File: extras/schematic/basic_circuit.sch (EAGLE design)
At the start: 17 parts, among them M1 ARDUINO-PRO-MINI-3.3V, Y1 32.768kHz

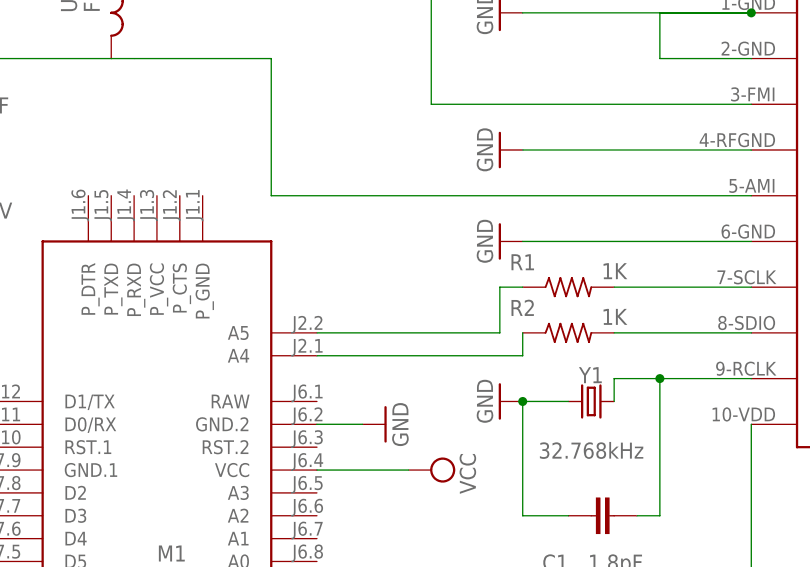
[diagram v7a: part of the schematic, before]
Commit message: BK1088 Arduino Library
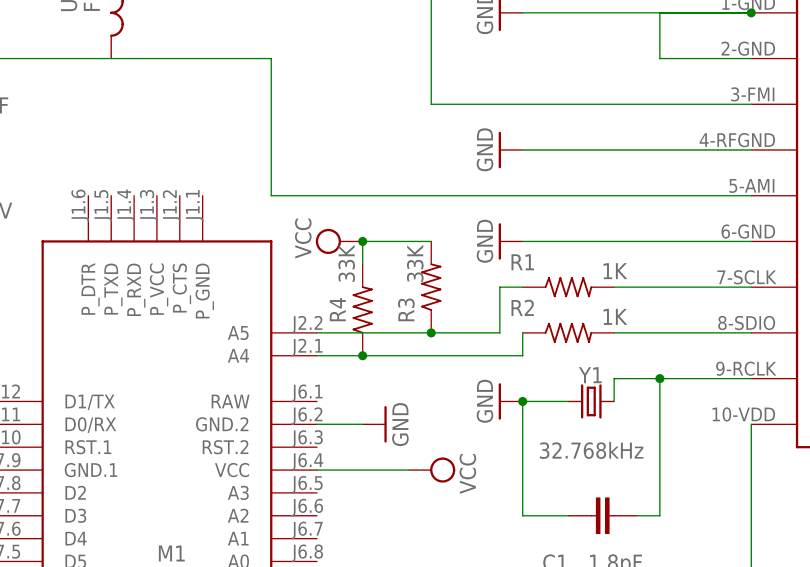
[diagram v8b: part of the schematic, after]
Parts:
- added R3, R4: 33K, Resistor:R-US_AXIAL-7.2MM-PITCH
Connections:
- net N$3: now also R4.1
- net N$4: now also R3.1
- net VCC: now also R3.2, R4.2
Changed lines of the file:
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@@
 <drawing>
 <settings>
-<setting alwaysvectorfont="yes"/>
+<setting alwaysvectorfont="no"/>
 <setting verticaltext="up"/>
 </settings>
@@
 <part name="C6" library="capacitor-wima" library_urn="urn:adsk.eagle:library:116" deviceset="C" device="5/3" package3d_urn="urn:adsk.eagle:package:5433/1" value="100nF"/>
 <part name="SW" library="discrete" library_urn="urn:adsk.eagle:library:211" deviceset="ANTENNA" device="" package3d_urn="urn:adsk.eagle:package:12928/1"/>
+<part name="R3" library="Resistor" library_urn="urn:adsk.eagle:library:16378527" deviceset="R-US" device="AXIAL-7.2MM-PITCH" package3d_urn="urn:adsk.eagle:package:16378561/2" technology="_" value="33K"/>
+<part name="R4" library="Resistor" library_urn="urn:adsk.eagle:library:16378527" deviceset="R-US" device="AXIAL-7.2MM-PITCH" package3d_urn="urn:adsk.eagle:package:16378561/2" technology="_" value="33K"/>
+<part name="SUPPLY3" library="supply2" library_urn="urn:adsk.eagle:library:372" deviceset="VCC" device=""/>
 </parts>
 <sheets>
@@
 <attribute name="NAME" x="-66.04" y="80.01" size="1.778" layer="95"/>
 <attribute name="VALUE" x="-60.96" y="73.66" size="1.778" layer="96"/>
+</instance>
+<instance part="R3" gate="G$1" x="12.7" y="45.72" smashed="yes" rot="R90">
+<attribute name="NAME" x="9.9314" y="43.18" size="1.778" layer="95" rot="R90" align="center"/>
+<attribute name="VALUE" x="10.922" y="48.26" size="1.778" layer="96" rot="R90" align="center"/>
+</instance>
+<instance part="R4" gate="G$1" x="5.08" y="43.18" smashed="yes" rot="R90">
+<attribute name="NAME" x="2.3114" y="43.18" size="1.778" layer="95" rot="R90" align="center"/>
+<attribute name="VALUE" x="3.302" y="48.26" size="1.778" layer="96" rot="R90" align="center"/>
+</instance>
+<instance part="SUPPLY3" gate="G$1" x="2.54" y="50.8" smashed="yes" rot="R90">
+<attribute name="VALUE" x="-0.635" y="48.895" size="1.778" layer="96" rot="R90"/>
 </instance>
 </instances>
@@
 <junction x="119.38" y="12.7"/>
 </segment>
+<segment>
+<pinref part="R4" gate="G$1" pin="2"/>
+<wire x1="5.08" y1="48.26" x2="5.08" y2="50.8" width="0.1524" layer="91"/>
+<pinref part="R3" gate="G$1" pin="2"/>
+<wire x1="5.08" y1="50.8" x2="12.7" y2="50.8" width="0.1524" layer="91"/>
+<pinref part="SUPPLY3" gate="G$1" pin="VCC"/>
+<junction x="5.08" y="50.8"/>
+</segment>
 </net>
 <net name="N$1" class="0">
@@
 <pinref part="M1" gate="G$1" pin="A4"/>
 <wire x1="22.86" y1="40.64" x2="22.86" y2="38.1" width="0.1524" layer="91"/>
-<wire x1="22.86" y1="38.1" x2="0" y2="38.1" width="0.1524" layer="91"/>
+<wire x1="22.86" y1="38.1" x2="5.08" y2="38.1" width="0.1524" layer="91"/>
+<pinref part="R4" gate="G$1" pin="1"/>
+<wire x1="5.08" y1="38.1" x2="0" y2="38.1" width="0.1524" layer="91"/>
+<junction x="5.08" y="38.1"/>
 </segment>
 </net>
@@
 <wire x1="20.32" y1="45.72" x2="20.32" y2="40.64" width="0.1524" layer="91"/>
 <pinref part="M1" gate="G$1" pin="A5"/>
-<wire x1="20.32" y1="40.64" x2="0" y2="40.64" width="0.1524" layer="91"/>
-</segment>
-</net>
+<wire x1="20.32" y1="40.64" x2="12.7" y2="40.64" width="0.1524" layer="91"/>
+<pinref part="R3" gate="G$1" pin="1"/>
+<wire x1="12.7" y1="40.64" x2="0" y2="40.64" width="0.1524" layer="91"/>
+<junction x="12.7" y="40.64"/>
+</segment>
+</net>
